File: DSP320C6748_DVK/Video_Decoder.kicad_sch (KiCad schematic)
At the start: 39 parts, among them IC1 TPS650250RHBR

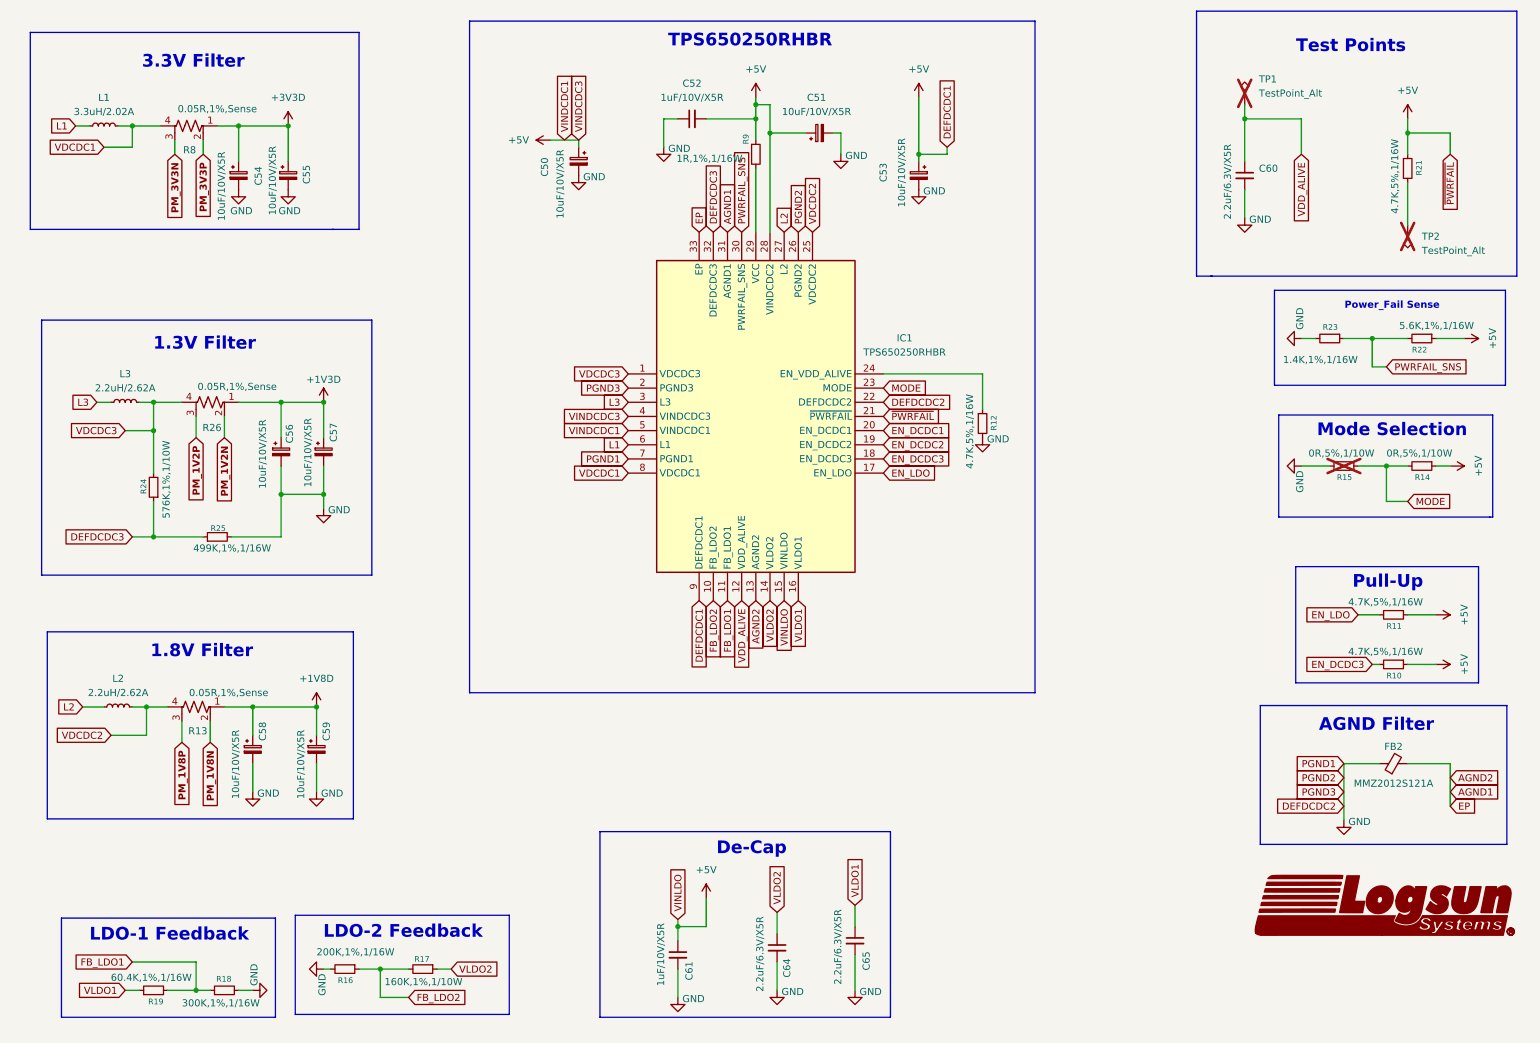
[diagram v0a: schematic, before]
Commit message: DDR_RAM and Video Decoder Schematic Added
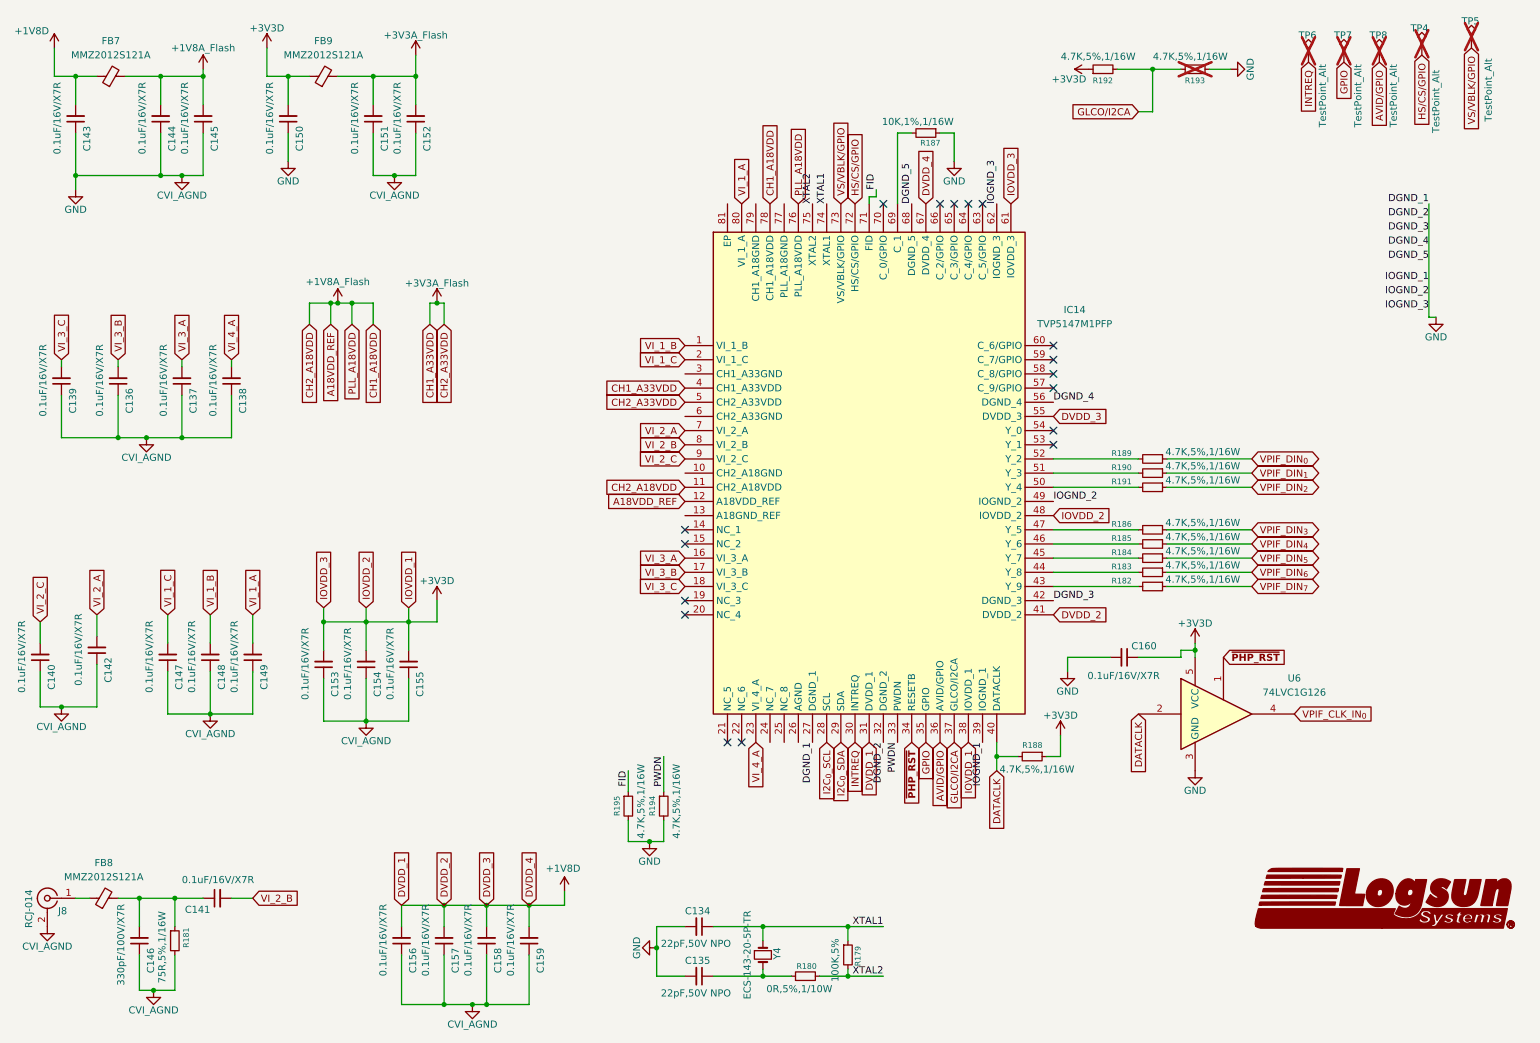
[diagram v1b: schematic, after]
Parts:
- removed C50, C51, C53, C54, C55, C56, C57, C58, C59: 10uF/10V/X5R, symbol Device:C_Polarized_Small
- removed C52, C61: 1uF/10V/X5R, symbol Device:C_Small
- removed C60, C64, C65: 2.2uF/6.3V/X5R, symbol Device:C_Small
- removed FB2: MMZ2012S121A, symbol Device:FerriteBead_Small
- removed IC1: TPS650250RHBR, TPS650250RHBR:QFN50P500X500X100-33N-D, symbol TPS650250RHBR:TPS650250RHBR
- removed L1: 3.3uH/2.02A, symbol Device:L_Small
- removed L2, L3: 2.2uH/2.62A, symbol Device:L_Small
- removed R10, R11, R12, R21: 4.7K,5%,1/16W, symbol Device:R_Small
- removed R13, R26, R8: 0.05R,1%,Sense, symbol Device:R_Shunt_US
- removed R14, R15: 0R,5%,1/10W, symbol Device:R_Small
- removed R16: 200K,1%,1/16W, symbol Device:R_Small
- removed R17: 160K,1%,1/10W, symbol Device:R_Small
- removed R18: 300K,1%,1/16W, symbol Device:R_Small
- removed R19: 60.4K,1%,1/16W, symbol Device:R_Small
- removed R22: 5.6K,1%,1/16W, symbol Device:R_Small
- removed R23: 1.4K,1%,1/16W, symbol Device:R_Small
- removed R24: 576K,1%,1/10W, symbol Device:R_Small
- removed R25: 499K,1%,1/16W, symbol Device:R_Small
- removed R9: 1R,1%,1/16W, symbol Device:R_Small
- removed TP1, TP2: TestPoint_Alt, symbol Connector:TestPoint_Alt
- added C134, C135: 22pF,50V NPO, symbol Device:C_Small
- added C136, C137, C138, C139, C140, C141, C142, C143, C144, C145, C147, C148, C149, C150, C151, C152, C153, C154, C155, C156, C157, C158, C159, C160: 0.1uF/16V/X7R, symbol Device:C_Small
- added C146: 330pF/100V/X7R, symbol Device:C_Small
- added FB7, FB8, FB9: MMZ2012S121A, symbol Device:FerriteBead_Small
- added IC14: TVP5147M1PFP, QFP50P1400X1400X120-81N, symbol TVP5147M1PFP:TVP5147M1PFP
- added J8: RCJ-014, symbol Connector:Conn_Coaxial
- added R179: 100K,5%, symbol Device:R_Small
- added R180: 0R,5%,1/10W, symbol Device:R_Small
- added R181: 75R,5%,1/16W, symbol Device:R_Small
- added R182, R183, R184, R185, R186, R188, R189, R190, R191, R192, R193, R194, R195: 4.7K,5%,1/16W, symbol Device:R_Small
- added R187: 10K,1%,1/16W, symbol Device:R_Small
- added TP4, TP5, TP6, TP7, TP8: TestPoint_Alt, symbol Connector:TestPoint_Alt
- added U6: 74LVC1G126, symbol 74xGxx:74LVC1G126
- added Y4: ECS-143-20-5P-TR, symbol Device:Crystal_Small
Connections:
- net +1V8D: now also C143.2, C156.2, C157.2, C158.2, C159.2, FB7.1, IC14.31 (DVDD_1), IC14.41 (DVDD_2), IC14.55 (DVDD_3), IC14.67 (DVDD_4)
- net +3V3D: now also C150.2, C153.2, C154.2, C155.2, C160.1, FB9.1, IC14.38 (IOVDD_1), IC14.48 (IOVDD_2), IC14.61 (IOVDD_3), R188.1, R192.1, U6.5 (VCC)
- new net: C135.1, R180.1, Y4.2
- new net: IC14.52 (Y_2), R189.2
- new net: IC14.51 (Y_3), R190.2
- new net: IC14.47 (Y_5), R186.2
- new net: IC14.43 (Y_9), R182.2
- new net: IC14.50 (Y_4), R191.2
- new net: IC14.69 (C_1), R187.2
- new net: C141.1, C146.2, FB8.2, R181.1
- new net: FB8.1, J8.1 (In)
- new net: IC14.46 (Y_6), R185.2
- new net: IC14.44 (Y_8), R183.2
- new net: IC14.45 (Y_7), R184.2
- new net +1V8A_Flash: C144.2, C145.2, FB7.2, IC14.11 (CH2_A18VDD), IC14.12 (A18VDD_REF), IC14.76 (PLL_A18VDD), IC14.78 (CH1_A18VDD)
- new net +3V3A_Flash: C151.2, C152.2, FB9.2, IC14.4 (CH1_A33VDD), IC14.5 (CH2_A33VDD)
- new net AVID/GPIO: IC14.36 (AVID/GPIO), TP8.1
- new net CVI_AGND: C134.2, C135.2, C136.1, C137.1, C138.1, C139.1, C140.1, C142.1, C143.1, C144.1, C145.1, C146.1, C147.1, C148.1, C149.1, C150.1, C151.1, C152.1, C153.1, C154.1, C155.1, C156.1, C157.1, C158.1, C159.1, C160.2, IC14.27 (DGND_1), IC14.32 (DGND_2), IC14.39 (IOGND_1), IC14.42 (DGND_3), IC14.49 (IOGND_2), IC14.56 (DGND_4), IC14.62 (IOGND_3), IC14.68 (DGND_5), J8.2 (Ext), R181.2, R187.1, R193.2, R194.2, R195.2, U6.3 (GND)
- new net DATACLK: IC14.40 (DATACLK), R188.2, U6.2
- new net FID: IC14.71 (FID), R195.1
- new net GLCO/I2CA: IC14.37 (GLCO/I2CA), R192.2, R193.1
- new net GPIO: IC14.35 (GPIO), TP7.1
- new net HS/CS/GPIO: IC14.72 (HS/CS/GPIO), TP4.1
- new net I2C_{0}_SCL: IC14.28 (SCL)
- new net I2C_{0}_SDA: IC14.29 (SDA)
- new net INTREQ: IC14.30 (INTREQ), TP6.1
- new net PWDN: IC14.33 (PWDN), R194.1
- new net VI_1_A: C149.2, IC14.80 (VI_1_A)
- new net VI_1_B: C148.2, IC14.1 (VI_1_B)
- new net VI_1_C: C147.2, IC14.2 (VI_1_C)
- new net VI_2_A: C142.2, IC14.7 (VI_2_A)
- new net VI_2_B: C141.2, IC14.8 (VI_2_B)
- new net VI_2_C: C140.2, IC14.9 (VI_2_C)
- new net VI_3_A: C137.2, IC14.16 (VI_3_A)
- new net VI_3_B: C136.2, IC14.17 (VI_3_B)
- new net VI_3_C: C139.2, IC14.18 (VI_3_C)
- new net VI_4_A: C138.2, IC14.23 (VI_4_A)
- new net VPIF_CLK_IN_{0}: U6.4
- new net VPIF_DIN_{0}: R189.1
- new net VPIF_DIN_{1}: R190.1
- new net VPIF_DIN_{2}: R191.1
- new net VPIF_DIN_{3}: R186.1
- new net VPIF_DIN_{4}: R185.1
- new net VPIF_DIN_{5}: R184.1
- new net VPIF_DIN_{6}: R183.1
- new net VPIF_DIN_{7}: R182.1
- new net VS/VBLK/GPIO: IC14.73 (VS/VBLK/GPIO), TP5.1
- new net XTAL1: C134.1, IC14.74 (XTAL1), R179.1, Y4.1
- new net XTAL2: IC14.75 (XTAL2), R179.2, R180.2
- new net ~{PHP_RST}: IC14.34 (RESETB), U6.1
- no-connect marks 0 -> 17
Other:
- note removed: "1.3V Filter"
- note removed: "1.8V Filter"
- note removed: "3.3V Filter"
- note removed: "AGND Filter"
- note removed: "De-Cap"
- note removed: "LDO-1 Feedback"
- note removed: "LDO-2 Feedback"
- note removed: "Mode Selection"
- note removed: "Power_Fail Sense"
- note removed: "Pull-Up"
- note removed: "TPS650250RHBR"
- note removed: "Test Points"
- company: Logsun Systems -> (none)
- title: DSP320C6748 DVK -> (none)

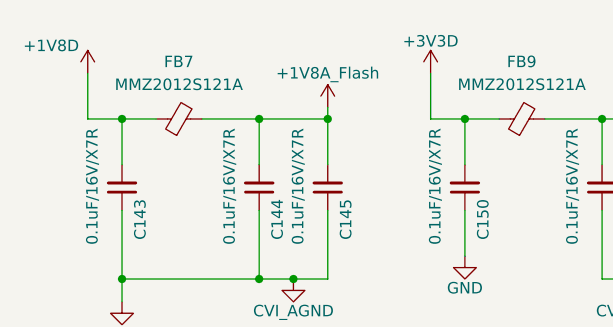
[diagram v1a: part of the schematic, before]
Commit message: Video and Audio Codec Schematic added
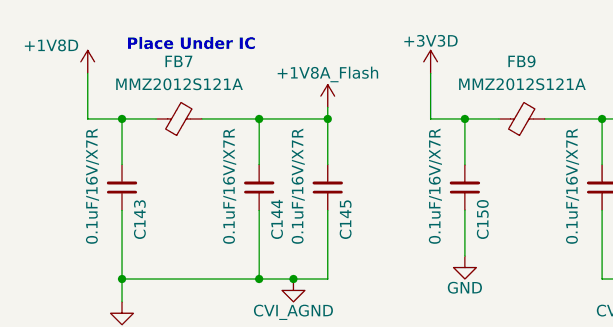
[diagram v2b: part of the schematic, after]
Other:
- note added: "Place Under IC"
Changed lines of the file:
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@@
 	(generator_version "10.0")
 	(paper "A4")
+	(text "Place Under IC"
+		(exclude_from_sim no)
+		(at 25.908 17.272 0)
+		(effects
+			(font
+				(size 1.27 1.27)
+				(thickness 0.254)
+				(bold yes)
+			)
+			(justify left)
+		)
+	)
 	(junction
 		(at 63.5 25.4)

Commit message: Connectors and mislleneous components added
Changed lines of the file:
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@@
 	(wire
 		(pts
-			(xy 267.97 68.58) (xy 267.97 48.26)
+			(xy 115.57 43.18) (xy 115.57 22.86)
 		)
 		(stroke
@@
 	(wire
 		(pts
-			(xy 269.24 68.58) (xy 267.97 68.58)
+			(xy 116.84 43.18) (xy 115.57 43.18)
 		)
 		(stroke
@@
 	)
 	(label "DGND_1"
-		(at 267.97 48.26 180)
+		(at 115.57 22.86 180)
 		(effects
 			(font
@@
 	)
 	(label "IOGND_3"
-		(at 267.97 67.31 180)
+		(at 115.57 41.91 180)
 		(effects
 			(font
@@
 	)
 	(label "IOGND_2"
-		(at 267.97 64.77 180)
+		(at 115.57 39.37 180)
 		(effects
 			(font
@@
 	)
 	(label "DGND_2"
-		(at 267.97 50.8 180)
+		(at 115.57 25.4 180)
 		(effects
 			(font
@@
 	)
 	(label "DGND_4"
-		(at 267.97 55.88 180)
+		(at 115.57 30.48 180)
 		(effects
 			(font
@@
 	)
 	(label "DGND_5"
-		(at 267.97 58.42 180)
+		(at 115.57 33.02 180)
 		(effects
 			(font
@@
 	)
 	(label "IOGND_1"
-		(at 267.97 62.23 180)
+		(at 115.57 36.83 180)
 		(effects
 			(font
@@
 	)
 	(label "DGND_3"
-		(at 267.97 53.34 180)
+		(at 115.57 27.94 180)
 		(effects
 			(font
@@
 	(symbol
 		(lib_id "power:GND")
-		(at 269.24 68.58 0)
+		(at 116.84 43.18 0)
 		(unit 1)
 		(body_style 1)
@@
 		(dnp no)
 		(property "Reference" "#PWR0264"
-			(at 269.24 74.93 0)
+			(at 116.84 49.53 0)
 			(hide yes)
 			(show_name no)
@@
 		)
 		(property "Value" "GND"
-			(at 269.24 72.136 0)
+			(at 116.84 46.736 0)
 			(show_name no)
 			(do_not_autoplace no)
@@
 		)
 		(property "Footprint" ""
-			(at 269.24 68.58 0)
+			(at 116.84 43.18 0)
 			(hide yes)
 			(show_name no)
@@
 		)
 		(property "Datasheet" ""
-			(at 269.24 68.58 0)
+			(at 116.84 43.18 0)
 			(hide yes)
 			(show_name no)
@@
 		)
 		(property "Description" "Power symbol creates a global label with name \"GND\" , ground"
-			(at 269.24 68.58 0)
+			(at 116.84 43.18 0)
 			(hide yes)
 			(show_name no)

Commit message: NAND Flash circuit and Power Testpoints added
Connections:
- net +1V8A_Flash renamed +1V8A_Video
- net +3V3A_Flash renamed +3V3A_Video
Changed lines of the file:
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@@
 			)
 		)
-		(property "Value" "+3V3A_Flash"
+		(property "Value" "+3V3A_Video"
 			(at 90.17 62.484 0)
 			(show_name no)
@@
 			)
 		)
-		(property "Value" "+3V3A_Flash"
+		(property "Value" "+3V3A_Video"
 			(at 86.36 18.034 0)
 			(show_name no)
@@
 			)
 		)
-		(property "Value" "+1V8A_Flash"
+		(property "Value" "+1V8A_Video"
 			(at 72.39 62.23 0)
 			(show_name no)
@@
 			)
 		)
-		(property "Value" "+1V8A_Flash"
+		(property "Value" "+1V8A_Video"
 			(at 48.26 20.32 0)
 			(show_name no)

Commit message: Whole Schematic Reannotation Done
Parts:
- renumbered C140 to C144, C139 to C145, C143 to C146, C142 to C147, C136 to C148, C146 to C149, C144 to C150, C147 to C151, C137 to C152, C145 to C153, C148 to C154, C141 to C155, C138 to C156, C149 to C157, C150 to C158, C153 to C159, C154 to C160, C151 to C161, C156 to C162, C155 to C163, C152 to C164, C157 to C165, C158 to C166, C159 to C167, C134 to C168, C135 to C169, C160 to C170, FB9 to FB10, FB7 to FB9, IC14 to IC15, R181 to R153, R195 to R154, R194 to R155, R180 to R156, R179 to R157, R187 to R158, R188 to R159, R192 to R160, R189 to R161, R190 to R162, R191 to R163, R186 to R164, R185 to R165, R184 to R166, R183 to R167, R182 to R168, R193 to R169, TP6 to TP11, TP7 to TP12, TP8 to TP13, TP4 to TP14, TP5 to TP15, U6 to U9

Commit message: Schematic Corrections-II Done
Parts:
- added JP2: Jumper_2_Open, symbol Jumper:Jumper_2_Open
- added R264: 1K,5%,1/16W, symbol Device:R_Small
- added R265: 20K,5%,1/16W, symbol Device:R_Small
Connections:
- net +1V8A_Video: now also JP2.1 (A)
- net +3V3D: now also R161.2, R162.2, R163.2, R164.2, R165.2, R166.2, R167.2, R168.2, R264.1, R265.1
- net CVI_AGND: now also IC15.10 (CH2_A18GND), IC15.13 (A18GND_REF), IC15.24 (NC_7), IC15.26 (AGND), IC15.3 (CH1_A33GND), IC15.6 (CH2_A33GND), IC15.77 (PLL_A18GND), IC15.79 (CH1_A18GND), IC15.81 (EP)
- net I2C_{0}_SCL: now also R264.2
- net I2C_{0}_SDA: now also R265.2
- net VPIF_DIN_{0}: now also IC15.52 (Y_2)
- net VPIF_DIN_{1}: now also IC15.51 (Y_3)
- net VPIF_DIN_{2}: now also IC15.50 (Y_4)
- net VPIF_DIN_{3}: now also IC15.47 (Y_5)
- net VPIF_DIN_{4}: now also IC15.46 (Y_6)
- net VPIF_DIN_{5}: now also IC15.45 (Y_7)
- net VPIF_DIN_{6}: now also IC15.44 (Y_8)
- net VPIF_DIN_{7}: now also IC15.43 (Y_9)
- net at IC15.25 (NC_8): now also JP2.2 (B)
- no-connect marks 17 -> 18
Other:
- moved on the sheet: R161, R162, R163, R164, R165, R166, R167, R168

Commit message: DC jack Replaced With Type-C, ADC and RTC section added
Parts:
- renumbered C144 to C146, C145 to C147, C146 to C148, C147 to C149, C148 to C150, C149 to C151, C150 to C152, C151 to C153, C152 to C154, C153 to C155, C154 to C156, C155 to C157, C156 to C158, C157 to C159, C158 to C160, C159 to C161, C160 to C162, C161 to C163, C162 to C164, C163 to C165, C164 to C166, C165 to C167, C166 to C168, C167 to C169, C168 to C170, C169 to C171, C170 to C172, FB8 to FB10, FB9 to FB11, FB10 to FB12, J8 to J9, R153 to R154, R154 to R155, R155 to R156, R156 to R157, R157 to R158, R158 to R159, R159 to R160, R160 to R161, R169 to R162, R161 to R163, R162 to R164, R163 to R165, R164 to R166, R165 to R167, R166 to R168, R167 to R169, R168 to R170, R264 to R171, R265 to R172

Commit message: Scheamtic Re-annotation done, Some footprints assigned
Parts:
- C149: renamed from C146; footprint (none) -> Capacitor_SMD:C_0603_1608Metric_Pad1.08x0.95mm_HandSolder
- C150: renamed from C147; footprint (none) -> Capacitor_SMD:C_0603_1608Metric_Pad1.08x0.95mm_HandSolder
- C151: renamed from C148; footprint (none) -> Capacitor_SMD:C_0603_1608Metric_Pad1.08x0.95mm_HandSolder
- C152: renamed from C149; footprint (none) -> Capacitor_SMD:C_0603_1608Metric_Pad1.08x0.95mm_HandSolder
- C153: renamed from C150; footprint (none) -> Capacitor_SMD:C_0603_1608Metric_Pad1.08x0.95mm_HandSolder
- C154: renamed from C151; footprint (none) -> Capacitor_SMD:C_0603_1608Metric_Pad1.08x0.95mm_HandSolder
- C155: renamed from C152; footprint (none) -> Capacitor_SMD:C_0603_1608Metric_Pad1.08x0.95mm_HandSolder
- C156: renamed from C153; footprint (none) -> Capacitor_SMD:C_0603_1608Metric_Pad1.08x0.95mm_HandSolder
- C157: renamed from C154; footprint (none) -> Capacitor_SMD:C_0603_1608Metric_Pad1.08x0.95mm_HandSolder
- C158: renamed from C155; footprint (none) -> Capacitor_SMD:C_0603_1608Metric_Pad1.08x0.95mm_HandSolder
- C159: renamed from C156; footprint (none) -> Capacitor_SMD:C_0603_1608Metric_Pad1.08x0.95mm_HandSolder
- C160: renamed from C157; footprint (none) -> Capacitor_SMD:C_0603_1608Metric_Pad1.08x0.95mm_HandSolder
- C161: renamed from C158; footprint (none) -> Capacitor_SMD:C_0603_1608Metric_Pad1.08x0.95mm_HandSolder
- C162: renamed from C159; footprint (none) -> Capacitor_SMD:C_0603_1608Metric_Pad1.08x0.95mm_HandSolder
- C163: renamed from C160; footprint (none) -> Capacitor_SMD:C_0603_1608Metric_Pad1.08x0.95mm_HandSolder
- C164: renamed from C161; footprint (none) -> Capacitor_SMD:C_0603_1608Metric_Pad1.08x0.95mm_HandSolder
- C165: renamed from C162; footprint (none) -> Capacitor_SMD:C_0603_1608Metric_Pad1.08x0.95mm_HandSolder
- C166: renamed from C163; footprint (none) -> Capacitor_SMD:C_0603_1608Metric_Pad1.08x0.95mm_HandSolder
- C167: renamed from C164; footprint (none) -> Capacitor_SMD:C_0603_1608Metric_Pad1.08x0.95mm_HandSolder
- C168: renamed from C165; footprint (none) -> Capacitor_SMD:C_0603_1608Metric_Pad1.08x0.95mm_HandSolder
- C169: renamed from C166; footprint (none) -> Capacitor_SMD:C_0603_1608Metric_Pad1.08x0.95mm_HandSolder
- C170: renamed from C167; footprint (none) -> Capacitor_SMD:C_0603_1608Metric_Pad1.08x0.95mm_HandSolder
- C171: renamed from C168; footprint (none) -> Capacitor_SMD:C_0603_1608Metric_Pad1.08x0.95mm_HandSolder
- C172: renamed from C169; footprint (none) -> Capacitor_SMD:C_0603_1608Metric_Pad1.08x0.95mm_HandSolder
- C173: renamed from C170; footprint (none) -> Capacitor_SMD:C_0603_1608Metric_Pad1.08x0.95mm_HandSolder
- C174: renamed from C171; footprint (none) -> Capacitor_SMD:C_0603_1608Metric_Pad1.08x0.95mm_HandSolder
- C175: renamed from C172; footprint (none) -> Capacitor_SMD:C_0603_1608Metric_Pad1.08x0.95mm_HandSolder
- FB11: renamed from FB10; footprint (none) -> Inductor_SMD:L_0805_2012Metric_Pad1.05x1.20mm_HandSolder
- FB12: renamed from FB11; footprint (none) -> Inductor_SMD:L_0805_2012Metric_Pad1.05x1.20mm_HandSolder
- FB13: renamed from FB12; footprint (none) -> Inductor_SMD:L_0805_2012Metric_Pad1.05x1.20mm_HandSolder
- R156: renamed from R154; footprint (none) -> Resistor_SMD:R_0603_1608Metric_Pad0.98x0.95mm_HandSolder
- R157: renamed from R155; footprint (none) -> Resistor_SMD:R_0603_1608Metric_Pad0.98x0.95mm_HandSolder
- R158: renamed from R156; footprint (none) -> Resistor_SMD:R_0603_1608Metric_Pad0.98x0.95mm_HandSolder
- R159: renamed from R157; footprint (none) -> Resistor_SMD:R_0603_1608Metric_Pad0.98x0.95mm_HandSolder
- R160: renamed from R158; footprint (none) -> Resistor_SMD:R_0603_1608Metric_Pad0.98x0.95mm_HandSolder
- R161: renamed from R159; footprint (none) -> Resistor_SMD:R_0603_1608Metric_Pad0.98x0.95mm_HandSolder
- R162: renamed from R160; footprint (none) -> Resistor_SMD:R_0603_1608Metric_Pad0.98x0.95mm_HandSolder
- R163: renamed from R161; footprint (none) -> Resistor_SMD:R_0603_1608Metric_Pad0.98x0.95mm_HandSolder
- R164: renamed from R162; footprint (none) -> Resistor_SMD:R_0603_1608Metric_Pad0.98x0.95mm_HandSolder
- R165: renamed from R163; footprint (none) -> Resistor_SMD:R_0603_1608Metric_Pad0.98x0.95mm_HandSolder
- R166: renamed from R164; footprint (none) -> Resistor_SMD:R_0603_1608Metric_Pad0.98x0.95mm_HandSolder
- R167: renamed from R165; footprint (none) -> Resistor_SMD:R_0603_1608Metric_Pad0.98x0.95mm_HandSolder
- R168: renamed from R166; footprint (none) -> Resistor_SMD:R_0603_1608Metric_Pad0.98x0.95mm_HandSolder
- R169: renamed from R167; footprint (none) -> Resistor_SMD:R_0603_1608Metric_Pad0.98x0.95mm_HandSolder
- R170: renamed from R168; footprint (none) -> Resistor_SMD:R_0603_1608Metric_Pad0.98x0.95mm_HandSolder
- R171: renamed from R169; footprint (none) -> Resistor_SMD:R_0603_1608Metric_Pad0.98x0.95mm_HandSolder
- R172: renamed from R170; footprint (none) -> Resistor_SMD:R_0603_1608Metric_Pad0.98x0.95mm_HandSolder
- R173: renamed from R171; footprint (none) -> Resistor_SMD:R_0603_1608Metric_Pad0.98x0.95mm_HandSolder
- R174: renamed from R172; footprint (none) -> Resistor_SMD:R_0603_1608Metric_Pad0.98x0.95mm_HandSolder
- TP11, TP12, TP13, TP14, TP15: footprint (none) -> TestPoint:TestPoint_Pad_D3.0mm
